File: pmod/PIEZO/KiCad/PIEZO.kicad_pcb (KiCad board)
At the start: 2 copper layers, 37 x 20 mm, 5 parts, among them J1 Conn_01x06_Pin

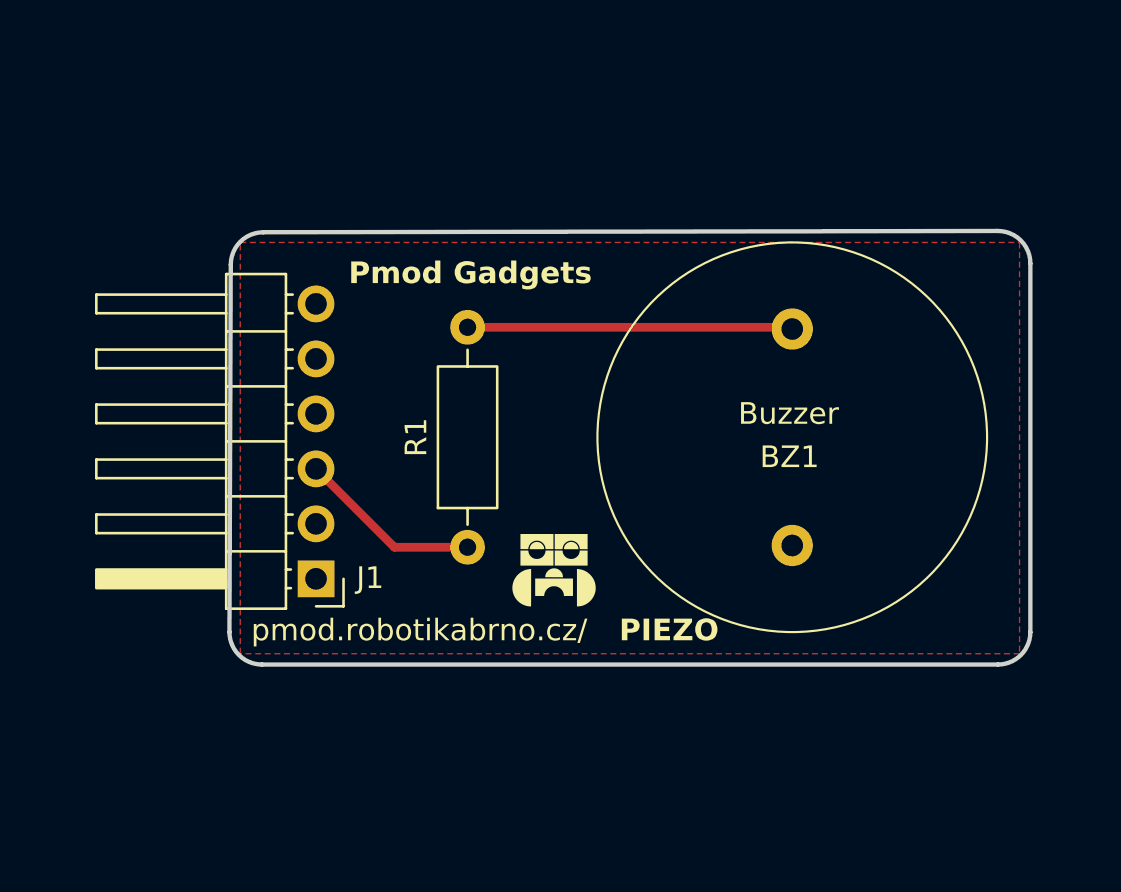
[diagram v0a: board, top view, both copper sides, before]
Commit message: added drill holes
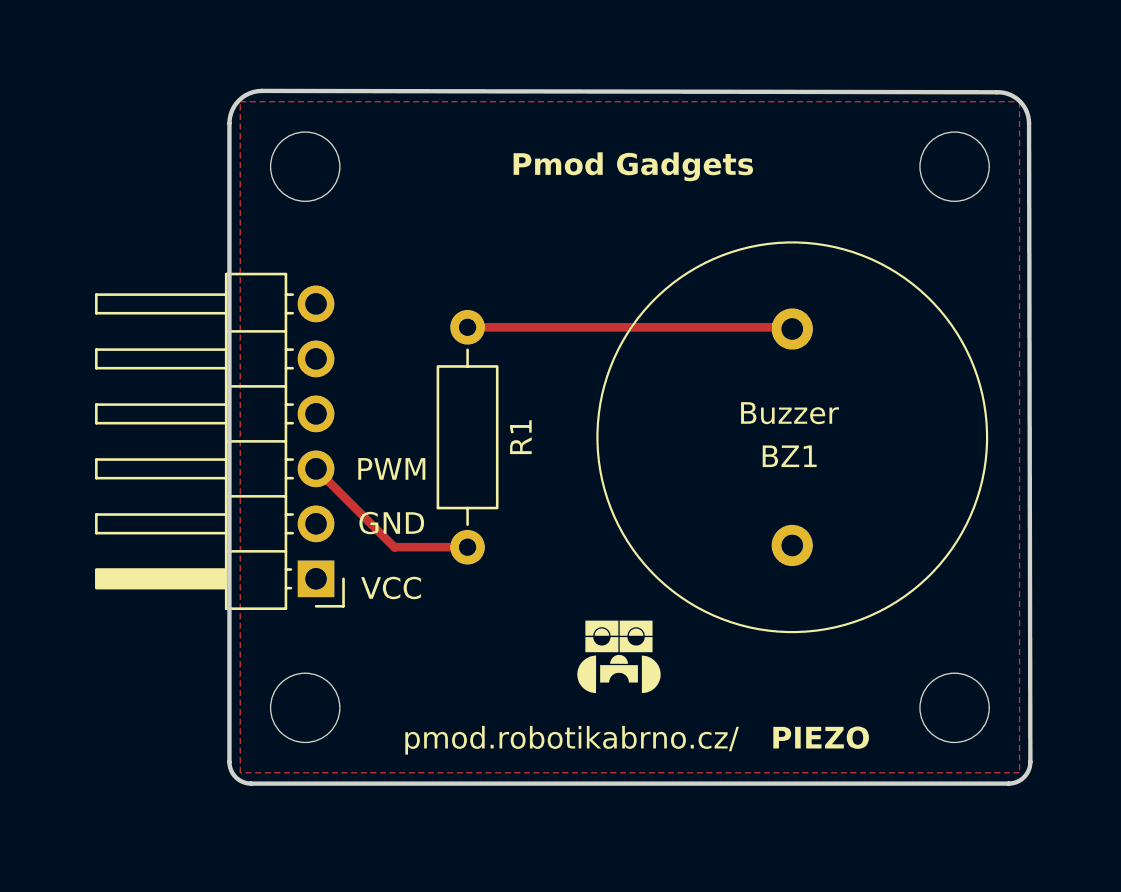
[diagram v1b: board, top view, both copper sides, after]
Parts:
- added REF**: MountingHole_3.2mm_M3, MountingHole:MountingHole_3.2mm_M3, F.Cu at (111.5, 50.5)
- added REF**: MountingHole_3.2mm_M3, MountingHole:MountingHole_3.2mm_M3, F.Cu at (81.5, 50.5)
- added REF**: MountingHole_3.2mm_M3, MountingHole:MountingHole_3.2mm_M3, F.Cu at (111.5, 75.5)
- added REF**: MountingHole_3.2mm_M3, MountingHole:MountingHole_3.2mm_M3, F.Cu at (81.5, 75.5)
- moved G*** 5.00 mm to (96.0, 73.0)
- renumbered J1 to VCC
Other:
- board size 37 x 20 mm -> 37 x 32 mm
- board text added: "GND"
- board text added: "PWM"

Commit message: minor changes and fixes
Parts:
- removed VCC: Conn_01x06_Pin, Connector_PinHeader_2.54mm:PinHeader_1x06_P2.54mm_Horizontal
- added J1: Conn_01x06_Pin, Connector_PinHeader_2.54mm:PinHeader_1x06_P2.54mm_Horizontal, F.Cu at (82.0, 69.5)
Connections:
- BZ1 pad 2: PWM -> Net-(BZ1-Pad2)
- R1 pad 2: PWM -> Net-(BZ1-Pad2)
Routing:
- net Net-(BZ1-Pad2): track 0.00 -> 15.0 mm
- net PWM: track 23.5 -> 9.84 mm
- net GND: vias 0 -> 14

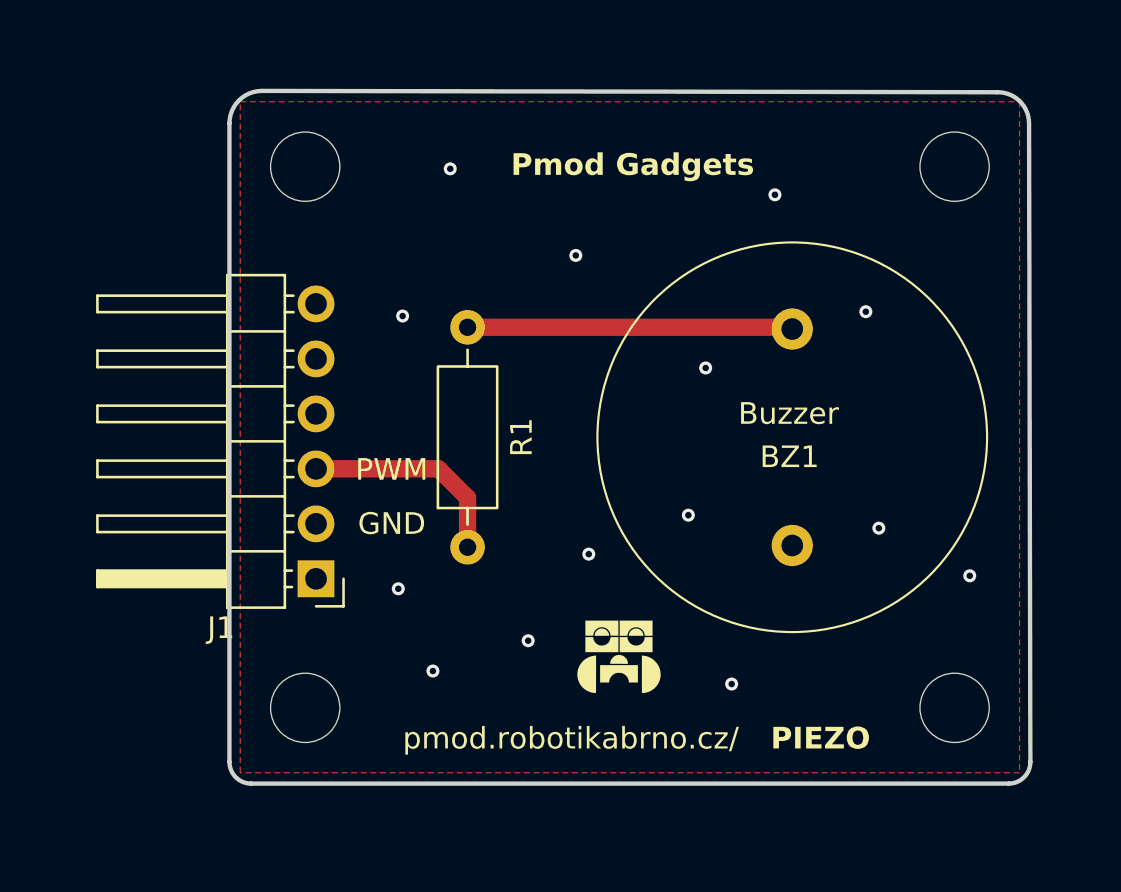
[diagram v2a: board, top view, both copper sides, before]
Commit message: Added hole description and dimensions
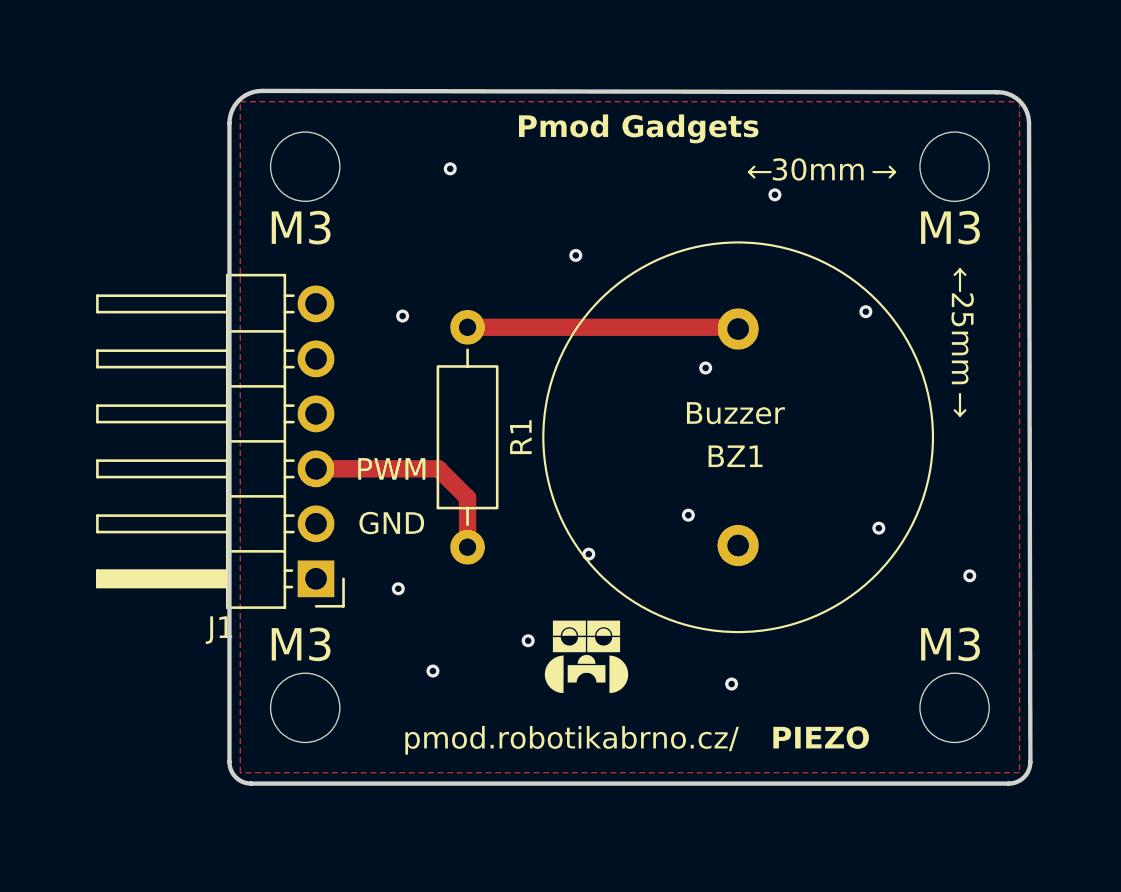
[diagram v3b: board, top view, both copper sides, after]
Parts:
- removed the G*** at (98.5, 63.0)
- moved BZ1 2.50 mm to (101.5, 63.0)
- moved G*** 1.50 mm to (94.5, 73.0)
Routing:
- net Net-(BZ1-Pad2): track 15.0 -> 12.5 mm
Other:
- board text added: "25mm"
- board text added: "30mm"
- board text added: "M3"

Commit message: minor fixes
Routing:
- added copper zone on B.Cu, net GND
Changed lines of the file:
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@@
 			(psa4output no)
 			(plot_black_and_white yes)
+			(plotinvisibletext no)
 			(sketchpadsonfab no)
 			(plotpadnumbers no)
@@
 		(net 1)
 		(net_name "GND")
-		(layer "F.Cu")
+		(layers "F.Cu" "B.Cu")
 		(hatch edge 0.5)
 		(connect_pads
@@
 		(polygon
 			(pts
-				(xy 78.5 47.5) (xy 114.5 47.5) (xy 114.5 78.5) (xy 78.5 78.5)
+				(xy 69.4 44.8) (xy 117.2 44.8) (xy 117.2 82) (xy 70.4 81.6)
 			)
 		)

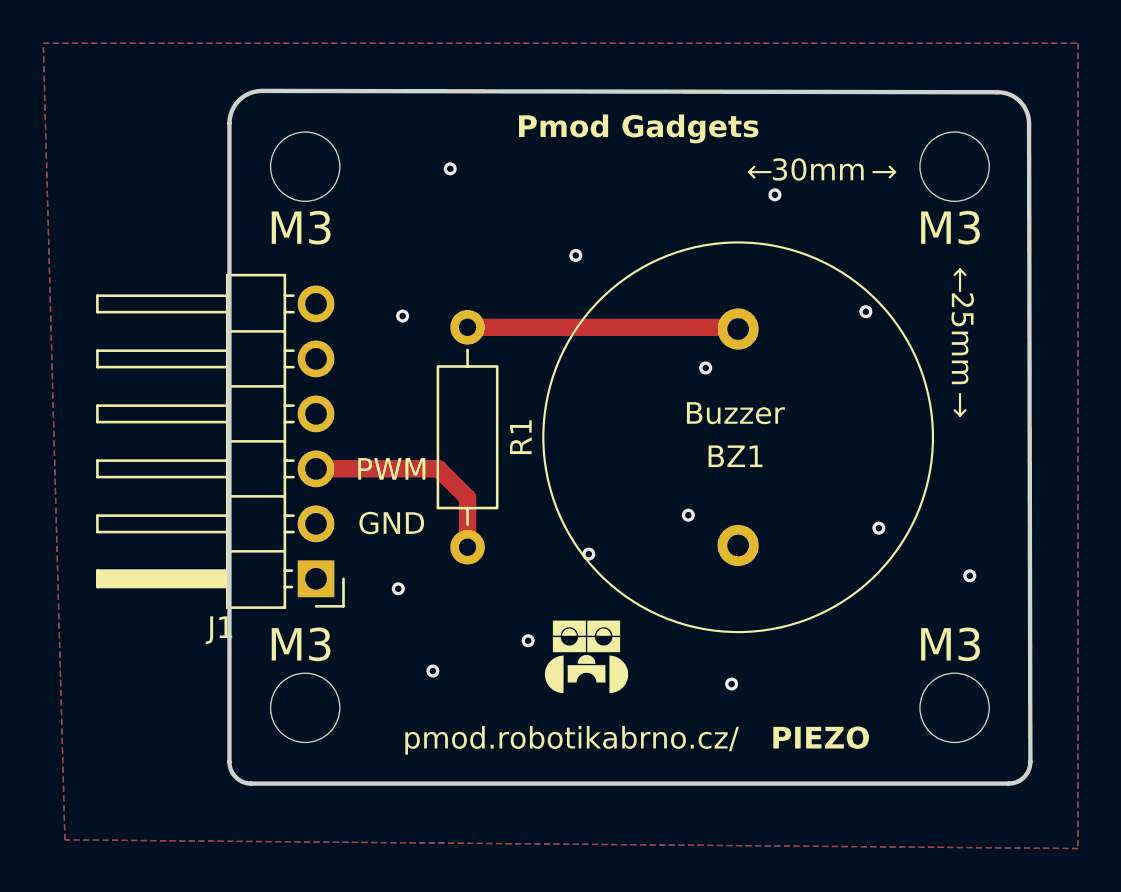
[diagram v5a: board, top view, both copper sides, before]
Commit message: modified the pcb to accept better piezo buzzer
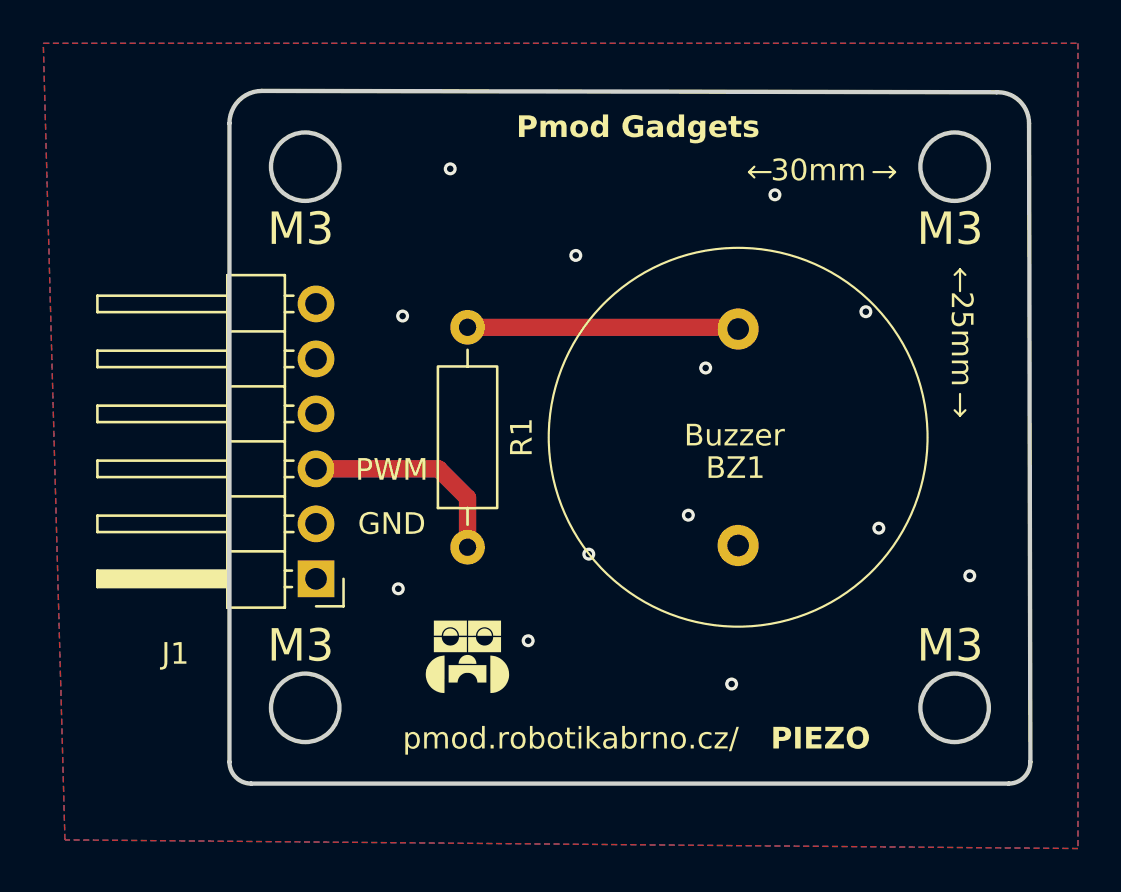
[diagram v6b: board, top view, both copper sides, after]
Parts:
- removed REF** (x4): MountingHole_3.2mm_M3, MountingHole:MountingHole_3.2mm_M3
- BZ1: value AZ-1740E-2P -> Buzzer; footprint Samacsys:AZ-1740E-2P -> PIEZO:buzzer
- moved G*** 5.50 mm to (89.0, 73.0)
- turned BZ1 to 0 degrees
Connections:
- BZ1 pad 1: GND -> Net-(BZ1-+)
- BZ1 pad 2: Net-(BZ1-Pad2) -> GND
- R1 pad 2: Net-(BZ1-Pad2) -> Net-(BZ1-+)
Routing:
- net Net-(BZ1-Pad2): track 12.5 -> 0.00 mm
- net Net-(BZ1-+): track 0.00 -> 12.5 mm
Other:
- outline, holes or cut-outs redrawn
- board text added: "Buzzer"

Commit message: added m3 holes and link to README
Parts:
- added REF**: MountingHole_3.2mm_M3, MountingHole:MountingHole_3.2mm_M3, F.Cu at (81.5, 75.5)
- added REF**: MountingHole_3.2mm_M3, MountingHole:MountingHole_3.2mm_M3, F.Cu at (111.5, 75.5)
- added REF**: MountingHole_3.2mm_M3, MountingHole:MountingHole_3.2mm_M3, F.Cu at (81.5, 50.5)
- added REF**: MountingHole_3.2mm_M3, MountingHole:MountingHole_3.2mm_M3, F.Cu at (111.5, 50.5)
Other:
- outline, holes or cut-outs redrawn

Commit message: jine piezo znovu
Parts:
- moved G*** 5.02 mm to (94.0, 72.5)
- moved REF** 5.00 mm to (106.5, 75.5)
- moved REF** 5.00 mm to (106.5, 50.5)
- moved BZ1 2.02 mm to (99.5, 63.0)
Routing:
- net Net-(BZ1-+): track 12.5 -> 11.7 mm
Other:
- board size 37 x 32 mm -> 32 x 32 mm
- board text removed: "30mm"
